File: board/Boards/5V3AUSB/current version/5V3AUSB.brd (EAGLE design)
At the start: 45.7 x 41.6 mm, 14 parts

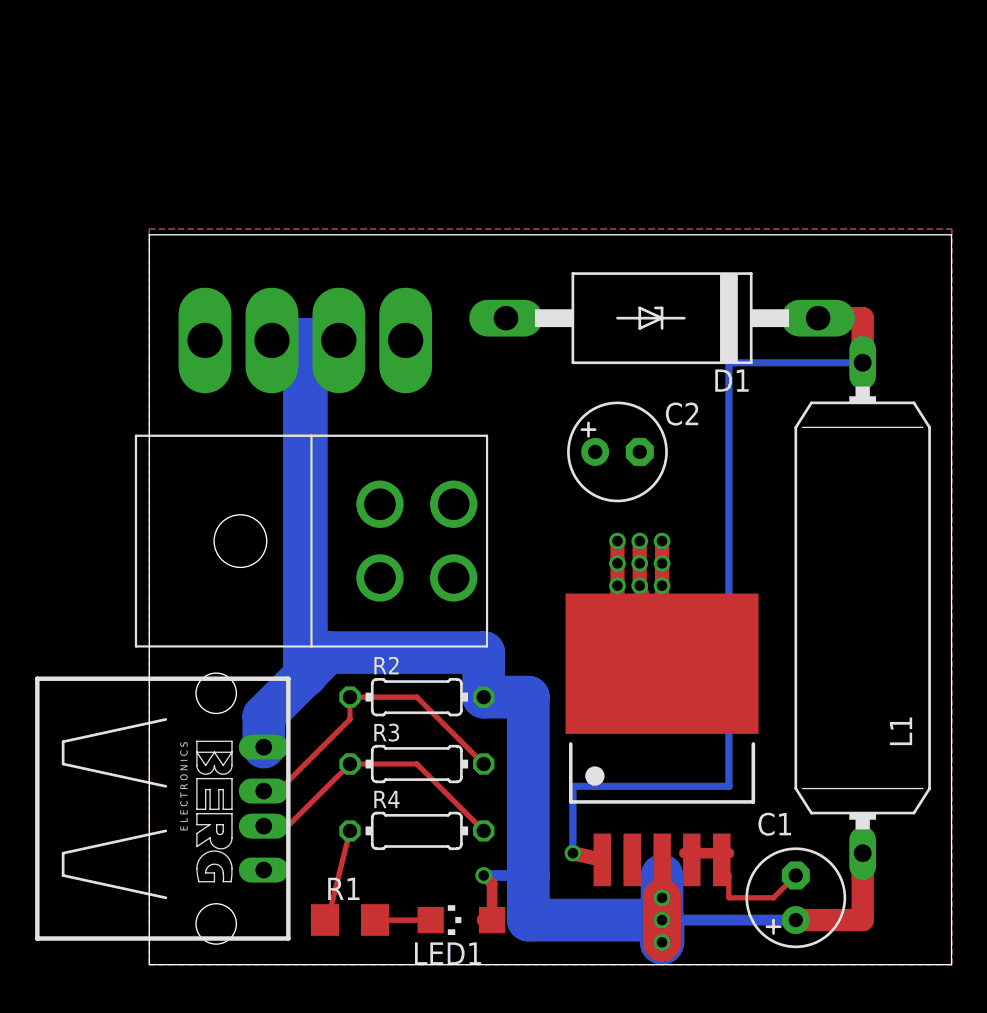
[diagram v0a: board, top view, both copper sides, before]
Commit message: rip up connectors before changing the pins around
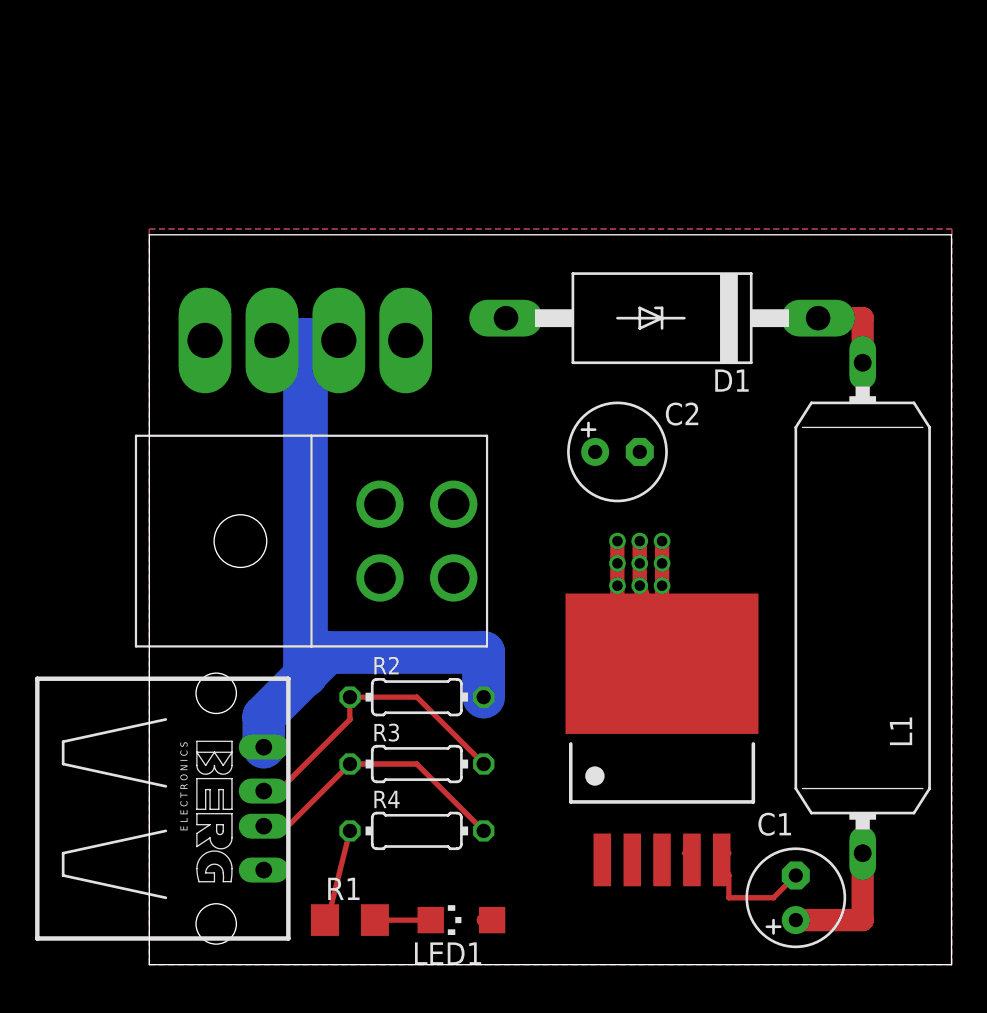
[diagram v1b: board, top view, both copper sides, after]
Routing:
- net N$2: track 51.3 -> 5.08 mm, vias 1 -> 0
- net N$3: track 95.5 -> 51.2 mm, vias 4 -> 0
- net GND: track 35.5 -> 33.0 mm
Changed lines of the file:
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@@
 <wire x1="10.16" y1="2.54" x2="10.008" y2="2.54" width="0.3048" layer="1"/>
 <wire x1="30.48" y1="6.35" x2="30.91" y2="5.97" width="0.3048" layer="1"/>
-<wire x1="33.02" y1="6.35" x2="30.48" y2="6.35" width="0.6096" layer="1"/>
 <wire x1="33.02" y1="6.35" x2="32.61" y2="5.97" width="0.3048" layer="1"/>
 <wire x1="35.56" y1="3.81" x2="36.83" y2="5.08" width="0.3048" layer="1"/>
@@
 <contactref element="TP1" pad="TP-2"/>
 <contactref element="TP2" pad="TP-2"/>
+<wire x1="32.61" y1="5.97" x2="30.91" y2="5.97" width="0" layer="19" extent="1-1"/>
 </signal>
 <signal name="N$2">
@@
 <contactref element="L1" pad="1"/>
 <contactref element="TO265-5" pad="1"/>
-<wire x1="24.13" y1="6.35" x2="25.81" y2="5.97" width="0.8128" layer="1"/>
-<via x="24.13" y="6.35" extent="1-16" drill="0.6"/>
 <wire x1="40.64" y1="34.29" x2="40.64" y2="36.83" width="1.27" layer="1"/>
 <wire x1="40.64" y1="36.83" x2="38.1" y2="36.83" width="1.27" layer="1"/>
-<wire x1="40.64" y1="34.29" x2="33.02" y2="34.29" width="0.4064" layer="16"/>
-<wire x1="33.02" y1="34.29" x2="33.02" y2="10.16" width="0.4064" layer="16"/>
-<wire x1="33.02" y1="10.16" x2="24.13" y2="10.16" width="0.4064" layer="16"/>
-<wire x1="24.13" y1="10.16" x2="24.13" y2="6.35" width="0.4064" layer="16"/>
+<wire x1="25.81" y1="5.97" x2="40.64" y2="34.29" width="0" layer="19" extent="1-1"/>
 </signal>
 <signal name="N$3">
@@
 <contactref element="LED1" pad="A"/>
 <wire x1="19.05" y1="2.54" x2="19.53" y2="2.54" width="0.8128" layer="1"/>
-<wire x1="29.21" y1="5.97" x2="29.21" y2="3.81" width="0.8128" layer="1"/>
-<wire x1="29.21" y1="3.81" x2="29.21" y2="2.54" width="2.1844" layer="1"/>
 <wire x1="6.52" y1="12.39" x2="6.52" y2="14.14" width="2.43" layer="16"/>
 <wire x1="6.52" y1="14.14" x2="8.89" y2="16.51" width="2.43" layer="16"/>
@@
 <wire x1="10.16" y1="17.78" x2="19.05" y2="17.78" width="2.43" layer="16"/>
 <wire x1="19.05" y1="17.78" x2="19.05" y2="15.24" width="2.43" layer="16"/>
-<wire x1="19.05" y1="15.24" x2="21.59" y2="15.24" width="2.43" layer="16"/>
-<wire x1="21.59" y1="15.24" x2="21.59" y2="5.08" width="2.43" layer="16"/>
-<wire x1="21.59" y1="5.08" x2="21.59" y2="2.54" width="2.43" layer="16"/>
-<wire x1="21.59" y1="2.54" x2="29.21" y2="2.54" width="2.43" layer="16"/>
-<via x="29.21" y="3.81" extent="1-16" drill="0.6"/>
-<via x="29.21" y="2.54" extent="1-16" drill="0.6"/>
-<wire x1="29.21" y1="2.54" x2="29.21" y2="5.08" width="2.43" layer="16"/>
-<wire x1="29.21" y1="2.54" x2="36.83" y2="2.54" width="0.6096" layer="16"/>
-<wire x1="19.53" y1="2.54" x2="19.53" y2="4.6" width="0.6096" layer="1"/>
-<wire x1="19.53" y1="4.6" x2="19.05" y2="5.08" width="0.6096" layer="1"/>
-<via x="19.05" y="5.08" extent="1-16" drill="0.6"/>
-<wire x1="19.05" y1="5.08" x2="21.59" y2="5.08" width="0.6096" layer="16"/>
-<wire x1="29.21" y1="2.54" x2="29.21" y2="1.27" width="2.1844" layer="1"/>
-<via x="29.21" y="1.27" extent="1-16" drill="0.6"/>
 <contactref element="TP1" pad="TP-1"/>
 <contactref element="TP2" pad="TP-1"/>
@@
 <wire x1="10.795" y1="35.56" x2="8.89" y2="35.56" width="2.54" layer="16"/>
 <wire x1="8.89" y1="35.56" x2="8.89" y2="16.51" width="2.54" layer="16"/>
-<wire x1="29.21" y1="1.27" x2="29.21" y2="2.54" width="2.54" layer="16"/>
+<wire x1="29.21" y1="5.97" x2="36.83" y2="2.54" width="0" layer="19" extent="1-1"/>
+<wire x1="19.53" y1="2.54" x2="29.21" y2="5.97" width="0" layer="19" extent="1-1"/>
+<wire x1="19.05" y1="15.24" x2="19.53" y2="2.54" width="0" layer="19" extent="1-1"/>
 </signal>
 <signal name="N$6">

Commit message: everything reworked except the power out
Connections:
- net GND: now also TO265-5.3; no longer TO265-5.4
- net N$1: now also TO265-5.1; no longer TO265-5.2
- net N$2: now also TO265-5.2; no longer TO265-5.1
- net N$3: now also TO265-5.4; no longer TO265-5.3
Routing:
- net N$2: track 5.08 -> 46.5 mm, vias 0 -> 1
- net N$3: track 51.2 -> 91.0 mm, vias 0 -> 1
- net GND: track 33.0 -> 44.2 mm
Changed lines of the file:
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@@
 <signal name="N$1">
 <contactref element="C2" pad="+"/>
-<contactref element="TO265-5" pad="2"/>
 <contactref element="U$1" pad="POWERL"/>
 <contactref element="U$1" pad="POWERR"/>
@@
 <vertex x="0" y="0"/>
 </polygon>
+<contactref element="TO265-5" pad="1"/>
 </signal>
 <signal name="GND">
@@
 <contactref element="D1" pad="A"/>
 <contactref element="TO265-5" pad="5"/>
-<contactref element="TO265-5" pad="4"/>
 <contactref element="X1" pad="4"/>
 <contactref element="R4" pad="1"/>
@@
 <wire x1="10.16" y1="2.54" x2="11.43" y2="7.62" width="0.3048" layer="1"/>
 <wire x1="10.16" y1="2.54" x2="10.008" y2="2.54" width="0.3048" layer="1"/>
-<wire x1="30.48" y1="6.35" x2="30.91" y2="5.97" width="0.3048" layer="1"/>
 <wire x1="33.02" y1="6.35" x2="32.61" y2="5.97" width="0.3048" layer="1"/>
 <wire x1="35.56" y1="3.81" x2="36.83" y2="5.08" width="0.3048" layer="1"/>
@@
 <contactref element="TP1" pad="TP-2"/>
 <contactref element="TP2" pad="TP-2"/>
-<wire x1="32.61" y1="5.97" x2="30.91" y2="5.97" width="0" layer="19" extent="1-1"/>
+<contactref element="TO265-5" pad="3"/>
+<contactref element="TO265-5" pad="3"/>
+<wire x1="29.21" y1="5.97" x2="29.21" y2="10.16" width="0.8128" layer="1"/>
+<wire x1="29.21" y1="10.16" x2="32.61" y2="10.16" width="0.8128" layer="1"/>
+<wire x1="32.61" y1="10.16" x2="32.61" y2="5.97" width="0.8128" layer="1"/>
 </signal>
 <signal name="N$2">
 <contactref element="D1" pad="C"/>
 <contactref element="L1" pad="1"/>
-<contactref element="TO265-5" pad="1"/>
 <wire x1="40.64" y1="34.29" x2="40.64" y2="36.83" width="1.27" layer="1"/>
 <wire x1="40.64" y1="36.83" x2="38.1" y2="36.83" width="1.27" layer="1"/>
-<wire x1="25.81" y1="5.97" x2="40.64" y2="34.29" width="0" layer="19" extent="1-1"/>
+<contactref element="TO265-5" pad="2"/>
+<wire x1="40.64" y1="34.29" x2="35.56" y2="34.29" width="0.8128" layer="16"/>
+<wire x1="35.56" y1="34.29" x2="35.56" y2="11.43" width="0.8128" layer="16"/>
+<wire x1="35.56" y1="11.43" x2="27.94" y2="11.43" width="0.8128" layer="16"/>
+<wire x1="27.51" y1="5.97" x2="27.94" y2="5.97" width="0.8128" layer="1"/>
+<wire x1="27.94" y1="5.97" x2="27.94" y2="11.43" width="0.8128" layer="1"/>
+<via x="27.94" y="11.43" extent="1-16" drill="0.6"/>
 </signal>
 <signal name="N$3">
 <contactref element="L1" pad="2"/>
 <contactref element="C1" pad="+"/>
-<contactref element="TO265-5" pad="3"/>
 <contactref element="R2" pad="2"/>
 <contactref element="X1" pad="1"/>
@@
 <wire x1="10.795" y1="35.56" x2="8.89" y2="35.56" width="2.54" layer="16"/>
 <wire x1="8.89" y1="35.56" x2="8.89" y2="16.51" width="2.54" layer="16"/>
-<wire x1="29.21" y1="5.97" x2="36.83" y2="2.54" width="0" layer="19" extent="1-1"/>
-<wire x1="19.53" y1="2.54" x2="29.21" y2="5.97" width="0" layer="19" extent="1-1"/>
-<wire x1="19.05" y1="15.24" x2="19.53" y2="2.54" width="0" layer="19" extent="1-1"/>
+<contactref element="TO265-5" pad="4"/>
+<wire x1="19.05" y1="15.24" x2="22.86" y2="15.24" width="2.54" layer="16"/>
+<wire x1="22.86" y1="15.24" x2="22.86" y2="5.08" width="2.54" layer="16"/>
+<wire x1="22.86" y1="5.08" x2="22.86" y2="2.54" width="2.54" layer="16"/>
+<wire x1="22.86" y1="2.54" x2="30.91" y2="2.54" width="2.54" layer="16"/>
+<wire x1="31.75" y1="2.54" x2="30.91" y2="2.54" width="2.54" layer="16"/>
+<wire x1="30.91" y1="2.54" x2="30.91" y2="5.97" width="2.54" layer="16"/>
+<wire x1="36.83" y1="2.54" x2="31.75" y2="2.54" width="1.778" layer="16"/>
+<wire x1="19.53" y1="2.54" x2="20.32" y2="2.54" width="0.4064" layer="1"/>
+<wire x1="20.32" y1="2.54" x2="20.32" y2="5.08" width="0.4064" layer="1"/>
+<wire x1="22.86" y1="5.08" x2="20.32" y2="5.08" width="0.4064" layer="16"/>
+<via x="20.32" y="5.08" extent="1-16" drill="0.6"/>
+<wire x1="30.91" y1="5.97" x2="30.91" y2="5.97" width="0" layer="19" extent="1-16"/>
 </signal>
 <signal name="N$6">

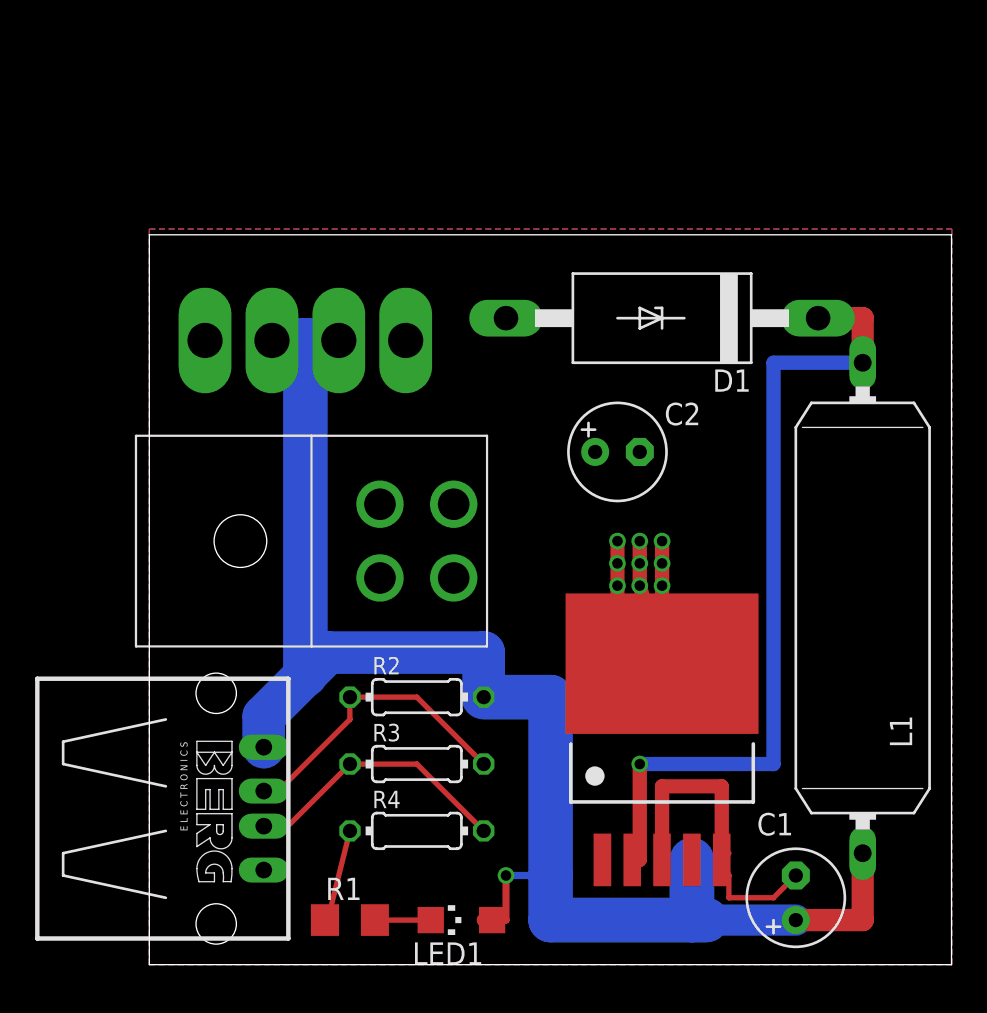
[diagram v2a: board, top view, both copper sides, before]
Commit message: changed - but it is still messed up. the thicknesses are wrong for some of the runs
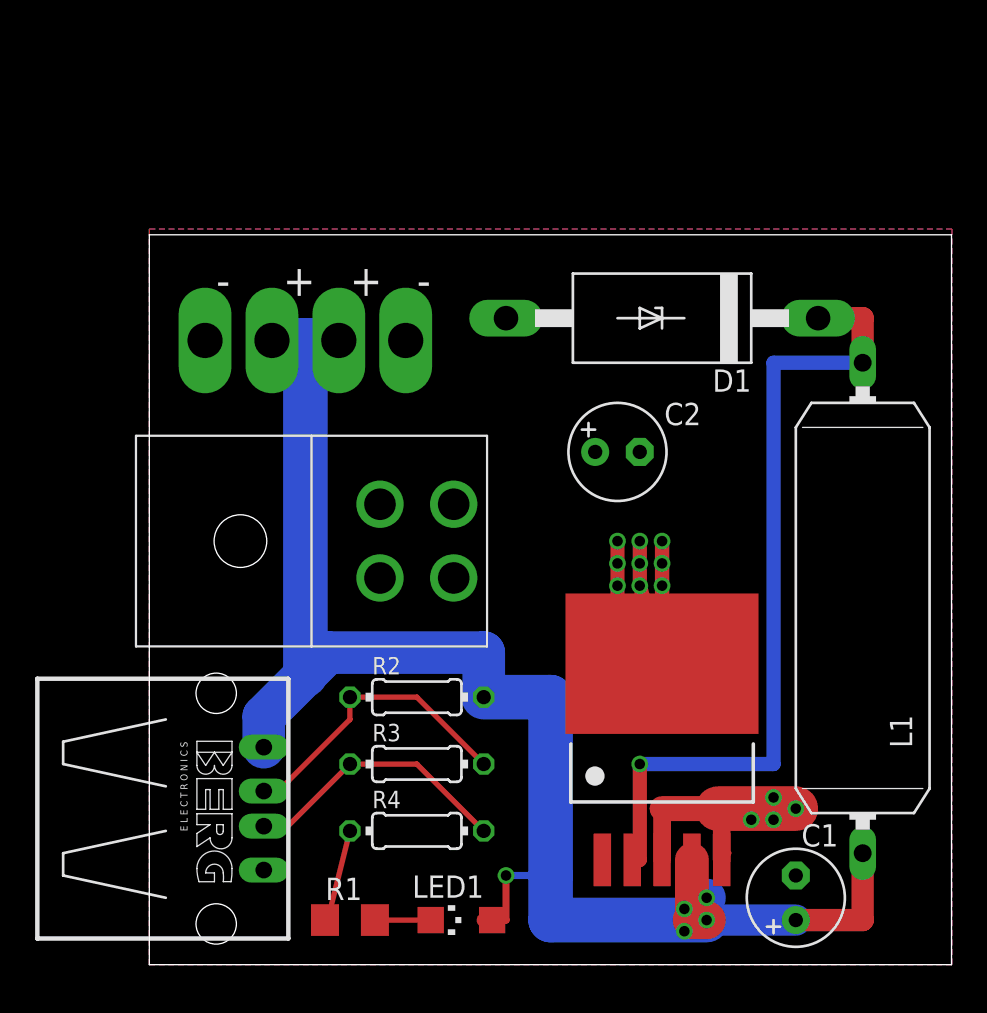
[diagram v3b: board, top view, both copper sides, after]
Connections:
- net GND renamed ASDAD
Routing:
- net ASDAD: track 44.2 -> 39.5 mm, vias 9 -> 13
- net N$3: track 91.0 -> 91.8 mm, vias 1 -> 2
- net N$8: track 0.00 -> 0.64 mm, vias 0 -> 1
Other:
- board text added: "+"
- board text added: "-"
- board text added: "5V 3A USB Supply v1.0 C.G & D.K hitchBOT - August 2014"
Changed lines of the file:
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@@
 <setting verticaltext="up"/>
 </settings>
-<grid distance="0.05" unitdist="inch" unit="inch" style="lines" multiple="1" display="no" altdistance="0.025" altunitdist="inch" altunit="inch"/>
+<grid distance="0.025" unitdist="inch" unit="inch" style="lines" multiple="1" display="no" altdistance="0.025" altunitdist="inch" altunit="inch"/>
 <layers>
 <layer number="1" name="Top" color="4" fill="1" visible="yes" active="yes"/>
@@
 <wire x1="45.7" y1="41.58" x2="0" y2="41.58" width="0" layer="20"/>
 <wire x1="0" y1="41.58" x2="0" y2="0" width="0" layer="20"/>
+<text x="7.62" y="38.1" size="1.778" layer="21">+</text>
+<text x="11.43" y="38.1" size="1.778" layer="21">+</text>
+<text x="3.81" y="38.1" size="1.778" layer="21">-</text>
+<text x="15.24" y="38.1" size="1.778" layer="21">-</text>
+<text x="43.18" y="33.655" size="1.27" layer="22" rot="MR270">5V 3A USB Supply v1.0
+C.G &amp; D.K
+hitchBOT - August 2014</text>
 </plain>
 <attributes>
@@
 <elements>
 <element name="C1" library="resistor" package="E2,5-6" value="220uF" x="36.83" y="3.81" smashed="yes" rot="R90">
-<attribute name="NAME" x="36.703" y="8.636" size="1.27" layer="25" ratio="10" rot="R180"/>
+<attribute name="NAME" x="39.243" y="8.001" size="1.27" layer="25" ratio="10" rot="R180"/>
 <attribute name="VALUE" x="44.323" y="2.667" size="1.27" layer="27" ratio="10" rot="R180"/>
 </element>
@@
 <attribute name="SPICEPREFIX" value="R" x="15.24" y="7.62" size="1.778" layer="27" display="off"/>
 </element>
-<element name="LED1" library="led" package="CHIPLED_1206" value="" x="17.78" y="2.54" rot="R90"/>
-<element name="R1" library="resistor" package="R1206" value="250" x="11.43" y="2.54"/>
+<element name="LED1" library="led" package="CHIPLED_1206" value="" x="17.78" y="2.54" smashed="yes" rot="R90">
+<attribute name="NAME" x="19.05" y="5.08" size="1.27" layer="25" rot="R180"/>
+<attribute name="VALUE" x="19.05" y="5.08" size="1.27" layer="27" rot="R180"/>
+</element>
+<element name="R1" library="resistor" package="R1206" value="250" x="11.43" y="2.54" smashed="yes">
+<attribute name="NAME" x="10.033" y="3.683" size="1.27" layer="25"/>
+</element>
 <element name="U$1" library="Molex" package="2X2MOLEX" value="2X2-MOLEX" x="15.24" y="24.13" rot="R270"/>
 <element name="TP1" library="testpad" package="P2-38-20" value="TP2P2-38-20" x="5.08" y="35.56" smashed="yes" rot="R180">
@@
 <contactref element="TO265-5" pad="1"/>
 </signal>
-<signal name="GND">
+<signal name="ASDAD">
 <contactref element="C2" pad="-"/>
 <contactref element="C1" pad="-"/>
@@
 <wire x1="10.16" y1="2.54" x2="10.008" y2="2.54" width="0.3048" layer="1"/>
 <wire x1="33.02" y1="6.35" x2="32.61" y2="5.97" width="0.3048" layer="1"/>
-<wire x1="35.56" y1="3.81" x2="36.83" y2="5.08" width="0.3048" layer="1"/>
-<wire x1="33.02" y1="3.81" x2="35.56" y2="3.81" width="0.3048" layer="1"/>
-<wire x1="33.02" y1="5.08" x2="33.02" y2="3.81" width="0.3048" layer="1"/>
-<wire x1="33.02" y1="5.08" x2="32.61" y2="5.97" width="0.3048" layer="1"/>
 <wire x1="26.67" y1="17.78" x2="26.67" y2="21.59" width="0.8128" layer="1"/>
 <wire x1="26.67" y1="21.59" x2="26.67" y2="22.86" width="0.8128" layer="1"/>
@@
 <contactref element="TO265-5" pad="3"/>
 <contactref element="TO265-5" pad="3"/>
-<wire x1="29.21" y1="5.97" x2="29.21" y2="10.16" width="0.8128" layer="1"/>
-<wire x1="29.21" y1="10.16" x2="32.61" y2="10.16" width="0.8128" layer="1"/>
-<wire x1="32.61" y1="10.16" x2="32.61" y2="5.97" width="0.8128" layer="1"/>
+<wire x1="29.21" y1="5.97" x2="29.21" y2="8.89" width="1.016" layer="1"/>
+<wire x1="29.21" y1="8.89" x2="32.385" y2="8.89" width="1.4224" layer="1"/>
+<wire x1="32.385" y1="8.89" x2="32.61" y2="8.89" width="1.016" layer="1"/>
+<wire x1="32.61" y1="8.89" x2="32.61" y2="5.97" width="1.016" layer="1"/>
+<wire x1="32.385" y1="8.89" x2="36.83" y2="8.89" width="2.54" layer="1"/>
+<via x="35.56" y="8.255" extent="1-16" drill="0.6"/>
+<via x="34.29" y="8.255" extent="1-16" drill="0.6"/>
+<via x="35.56" y="9.525" extent="1-16" drill="0.6"/>
+<via x="36.83" y="8.89" extent="1-16" drill="0.6"/>
 </signal>
 <signal name="N$2">
@@
 <wire x1="22.86" y1="15.24" x2="22.86" y2="5.08" width="2.54" layer="16"/>
 <wire x1="22.86" y1="5.08" x2="22.86" y2="2.54" width="2.54" layer="16"/>
-<wire x1="22.86" y1="2.54" x2="30.91" y2="2.54" width="2.54" layer="16"/>
-<wire x1="31.75" y1="2.54" x2="30.91" y2="2.54" width="2.54" layer="16"/>
-<wire x1="30.91" y1="2.54" x2="30.91" y2="5.97" width="2.54" layer="16"/>
+<wire x1="22.86" y1="2.54" x2="31.75" y2="2.54" width="2.54" layer="16"/>
 <wire x1="36.83" y1="2.54" x2="31.75" y2="2.54" width="1.778" layer="16"/>
 <wire x1="19.53" y1="2.54" x2="20.32" y2="2.54" width="0.4064" layer="1"/>
@@
 <wire x1="22.86" y1="5.08" x2="20.32" y2="5.08" width="0.4064" layer="16"/>
 <via x="20.32" y="5.08" extent="1-16" drill="0.6"/>
-<wire x1="30.91" y1="5.97" x2="30.91" y2="5.97" width="0" layer="19" extent="1-16"/>
+<via x="31.75" y="2.54" extent="1-16" drill="0.6"/>
+<wire x1="31.75" y1="2.54" x2="30.91" y2="2.54" width="2.1844" layer="1"/>
+<wire x1="30.91" y1="2.54" x2="30.91" y2="5.97" width="1.9304" layer="1"/>
 </signal>
 <signal name="N$6">
@@
 <wire x1="16.51" y1="2.54" x2="16.03" y2="2.54" width="0.3048" layer="1"/>
 </signal>
+<signal name="N$4">
+<via x="30.48" y="3.175" extent="1-16" drill="0.6"/>
+</signal>
+<signal name="N$8">
+<via x="31.75" y="3.81" extent="1-16" drill="0.6"/>
+<wire x1="31.115" y1="3.81" x2="31.75" y2="3.81" width="2.1844" layer="16"/>
+</signal>
+<signal name="N$9">
+<via x="30.48" y="1.905" extent="1-16" drill="0.6"/>
+</signal>
 </signals>
+<errors>
+</errors>
 </board>
 </drawing>
+<compatibility>
+<note version="6.3" minversion="6.2.2" severity="warning">
+Since Version 6.2.2 text objects can contain more than one line,
+which will not be processed correctly with this version.
+</note>
+</compatibility>
 </eagle>

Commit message: changed the name of pad - ready to delete
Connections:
- net ASDAD renamed GND
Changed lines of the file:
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@@
 <contactref element="TO265-5" pad="1"/>
 </signal>
-<signal name="ASDAD">
+<signal name="GND">
 <contactref element="C2" pad="-"/>
 <contactref element="C1" pad="-"/>
